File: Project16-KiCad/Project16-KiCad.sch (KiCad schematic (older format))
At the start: 33 parts, among them P1 2 AA Batt, P2 ICSP, P3 PWM1, P4 PWM2, P5 Serial Debug, Q1 SI2315, SW1 SW_PUSH, SW2 SW_PUSH, SW3 SW_PUSH, SW4 SW_PUSH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

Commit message: V0.3 Prototype
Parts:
- added C6: 0.1uF, Capacitors_SMD:C_1206_HandSoldering, symbol C
- LED3, LED4: footprint (none) -> Project16:7SegLedDisp4Digit
- SW1, SW2, SW3, SW4: footprint (none) -> Project16:Btn12x12
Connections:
- wire segments 281 -> 243

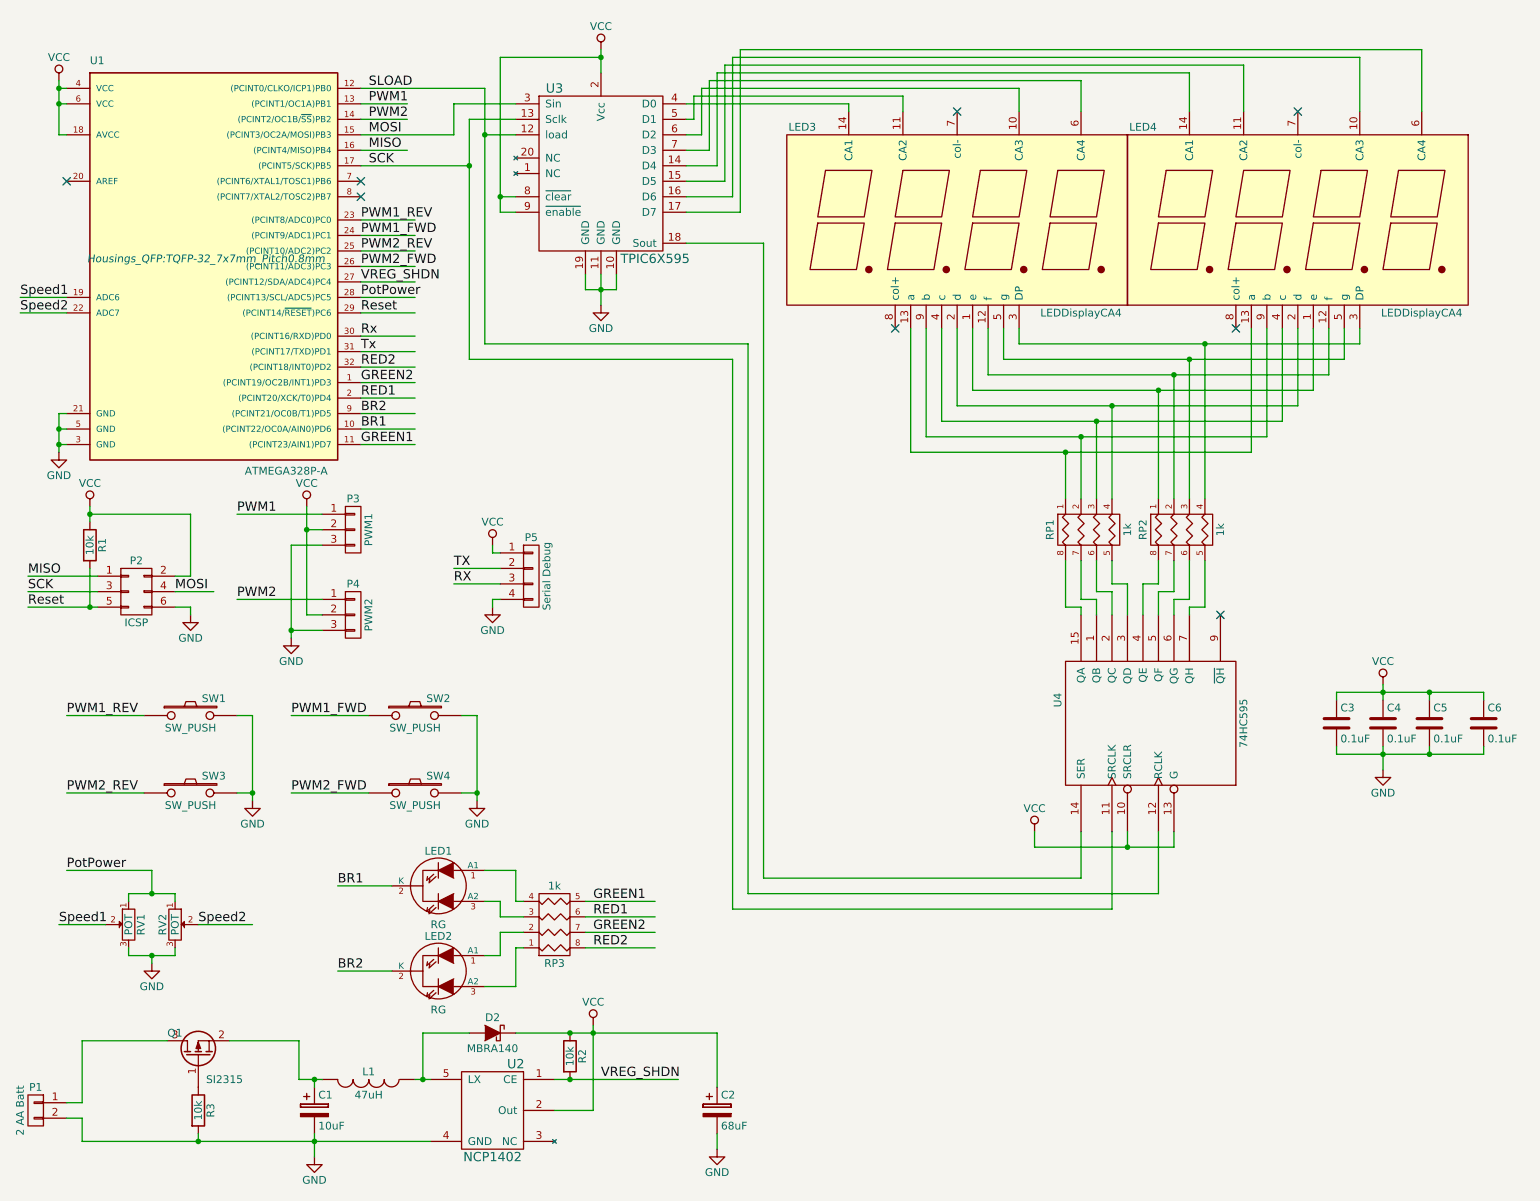
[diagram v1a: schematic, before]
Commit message: Improved boost converter, Added crystal.
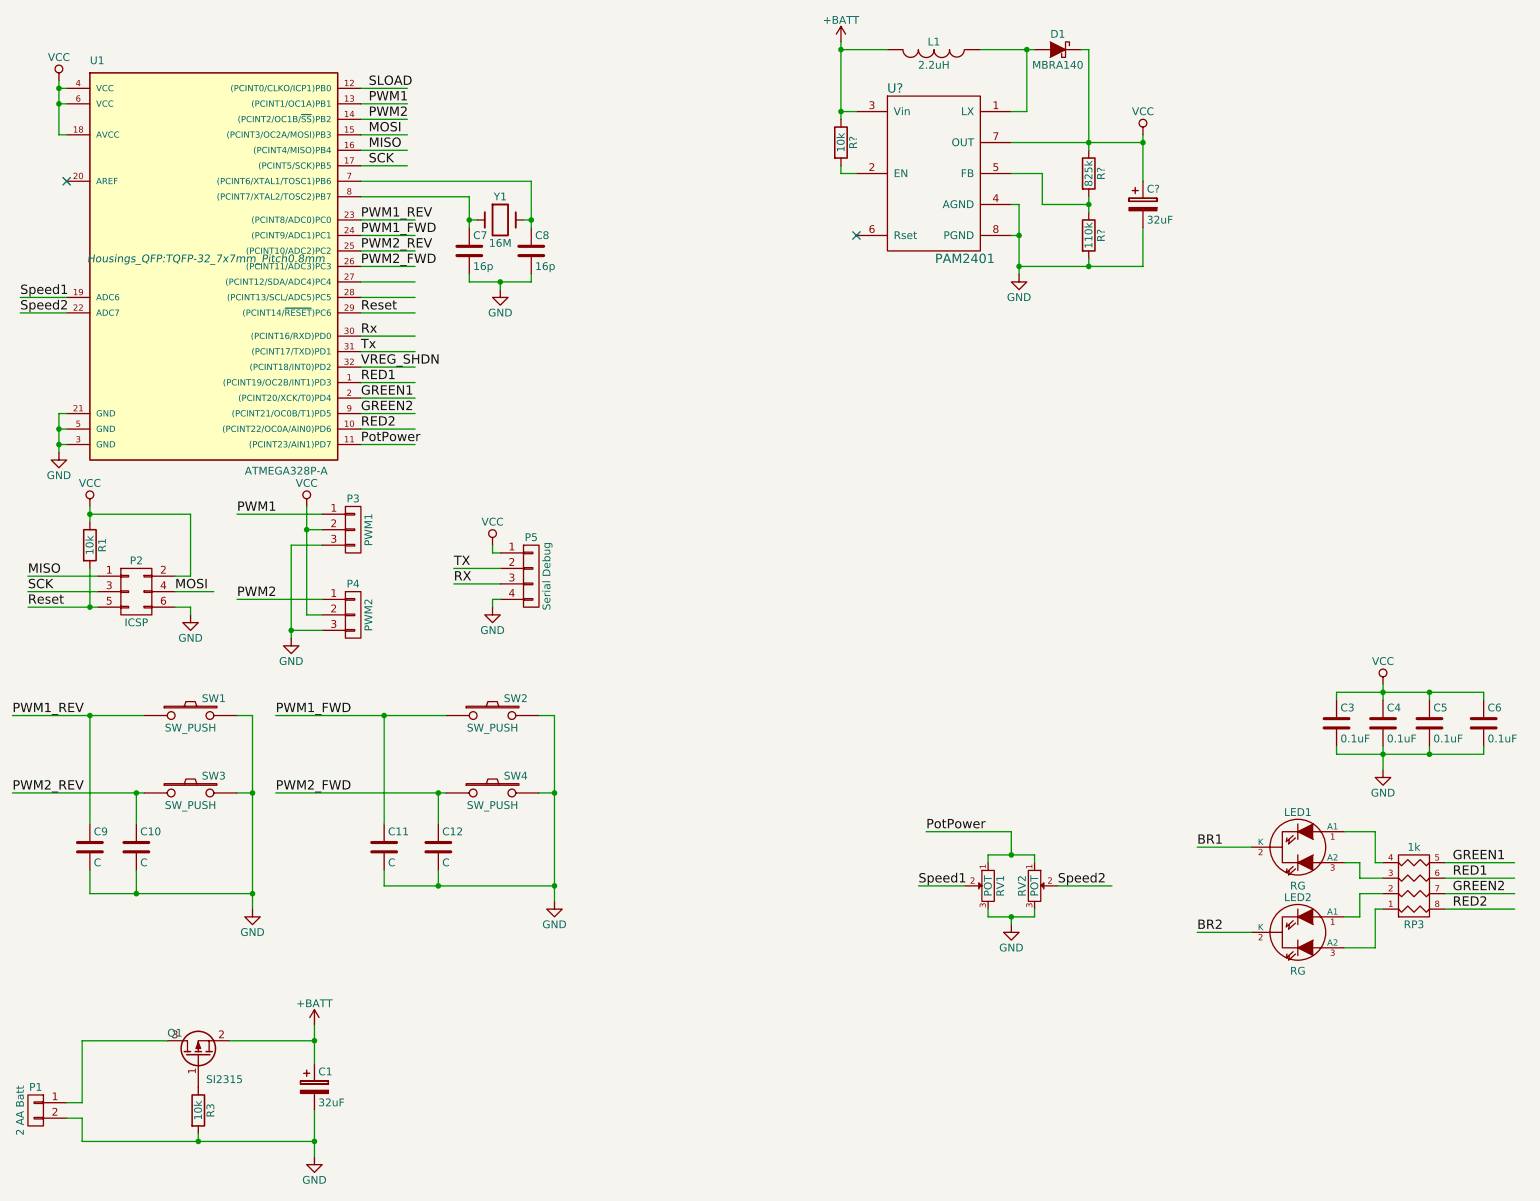
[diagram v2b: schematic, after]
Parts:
- removed C2: 68uF, Capacitors_ThroughHole:CP_Radial_D6.3mm_P2.50mm, symbol CP
- removed D2: MBRA140, Diodes_SMD:D_SMA_Handsoldering, symbol D_Schottky
- removed LED3, LED4: LEDDisplayCA4, Project16:7SegLedDisp4Digit, symbol LEDDisplayCA4
- removed R2: 10k, Resistors_SMD:R_1206_HandSoldering, symbol R
- removed RP1, RP2: 1k, Resistors_SMD:R_Array_Convex_4x1206, symbol R_PACK4
- removed U2: NCP1402, TO_SOT_Packages_SMD:SOT-23-5_HandSoldering, symbol NCP1402
- removed U3: TPIC6X595, Housings_SOIC:SOIC-20W_7.5x12.8mm_Pitch1.27mm, symbol TPIC6X595
- removed U4: 74HC595, Housings_SOIC:SOIC-16_3.9x9.9mm_Pitch1.27mm, symbol 74HC595
- added C10, C11, C12, C9: C, symbol C
- added C7, C8: 16p, symbol C
- added C?: 32uF, symbol CP
- added D1: MBRA140, symbol D_Schottky
- added R?: 10k, symbol R
- added R?: 825k, symbol R
- added R?: 110k, symbol R
- added U?: PAM2401, symbol PAM2401
- added Y1: 16M, symbol Crystal
- C1: value 10uF -> 32uF
- L1: value 47uH -> 2.2uH; footprint Choke_Toroid_ThroughHole:Choke_Toroid_5x10mm_Vertical -> (none)
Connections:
- net labels added: +BATT
- wire segments 243 -> 157
- no-connect marks 8 -> 2
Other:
- moved on the sheet: C1, LED1, LED2, RP3, RV1, RV2, SW2, SW4

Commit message: added lcd display
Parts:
- added DS1: LCD16X2, WC1602A, symbol LCD16X2
- added R10: 10k, symbol R
- added U3: 74HC595, symbol 74HC595
- gave numbers to parts that had none: 1
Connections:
- net labels added: V0
- wire segments 157 -> 190
- no-connect marks 2 -> 6

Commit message: Added License Statement, Minor circuit corrections
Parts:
- removed P5: Serial Debug, Pin_Headers:Pin_Header_Straight_1x04_Pitch2.54mm, symbol CONN_01X04
- removed RP3: 1k, Resistors_SMD:R_Array_Convex_4x1206, symbol R_PACK4
- added P5: Serial Debug, Pin_Headers:Pin_Header_Angled_1x06_Pitch2.54mm, symbol CONN_01X06
- added R6, R7, R8, R9: 1k, Resistors_SMD:R_1206_HandSoldering, symbol R
- C1: footprint Capacitors_ThroughHole:CP_Radial_D5.0mm_P2.00mm -> Capacitors_Tantalum_SMD:CP_Tantalum_Case-B_EIA-3528-21_Hand
- C10, C11, C12, C9: footprint (none) -> Capacitors_SMD:C_1206_HandSoldering
- C2: renamed from C?; footprint (none) -> Capacitors_Tantalum_SMD:CP_Tantalum_Case-B_EIA-3528-21_Hand
- C7, C8: footprint (none) -> Capacitors_SMD:C_0805_HandSoldering
- D1: footprint (none) -> Diodes_SMD:D_SMA_Handsoldering
- DS1: footprint WC1602A -> Display:WC1602A
- L1: footprint (none) -> Capacitors_SMD:C_1210_HandSoldering
- R10: footprint (none) -> Resistors_SMD:R_1206_HandSoldering
- R2, R4, R5: renamed from R?; footprint (none) -> Resistors_SMD:R_1206_HandSoldering
- U2: footprint (none) -> Housings_SSOP:MSOP-8_3x3mm_Pitch0.65mm
- U3: footprint (none) -> Housings_SOIC:SOIC-16_3.9x9.9mm_Pitch1.27mm
- Y1: footprint (none) -> Crystals:Crystal_SMD_HC49-SD_HandSoldering
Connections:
- net labels removed: BR1, BR2
- wire segments 190 -> 182
- no-connect marks 6 -> 9
